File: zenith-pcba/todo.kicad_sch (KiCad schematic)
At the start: 2 parts, among them U1 XC7A50T-CSG325, U2 K4B4G1646E-BCNB

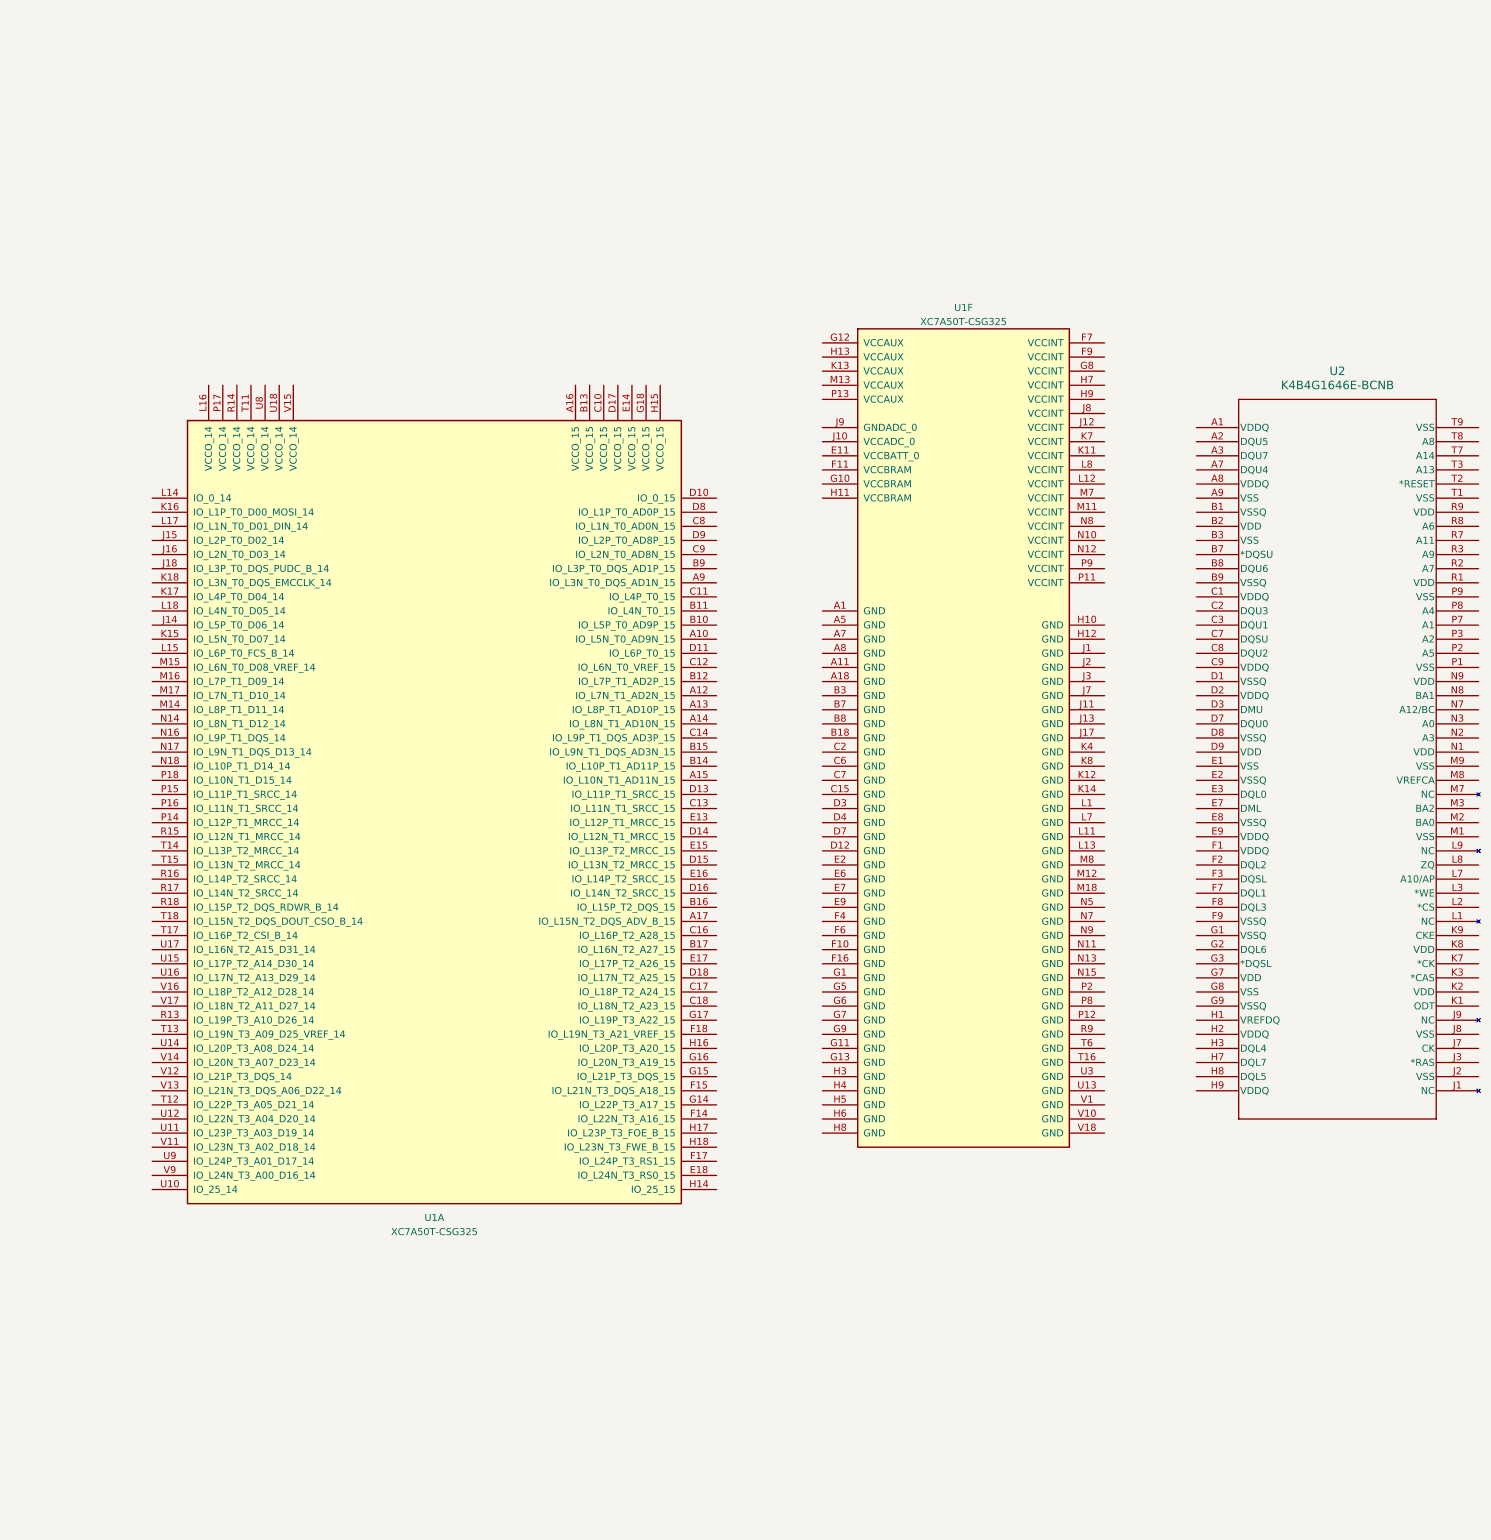
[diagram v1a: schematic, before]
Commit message: chore(pcba): import din connectors
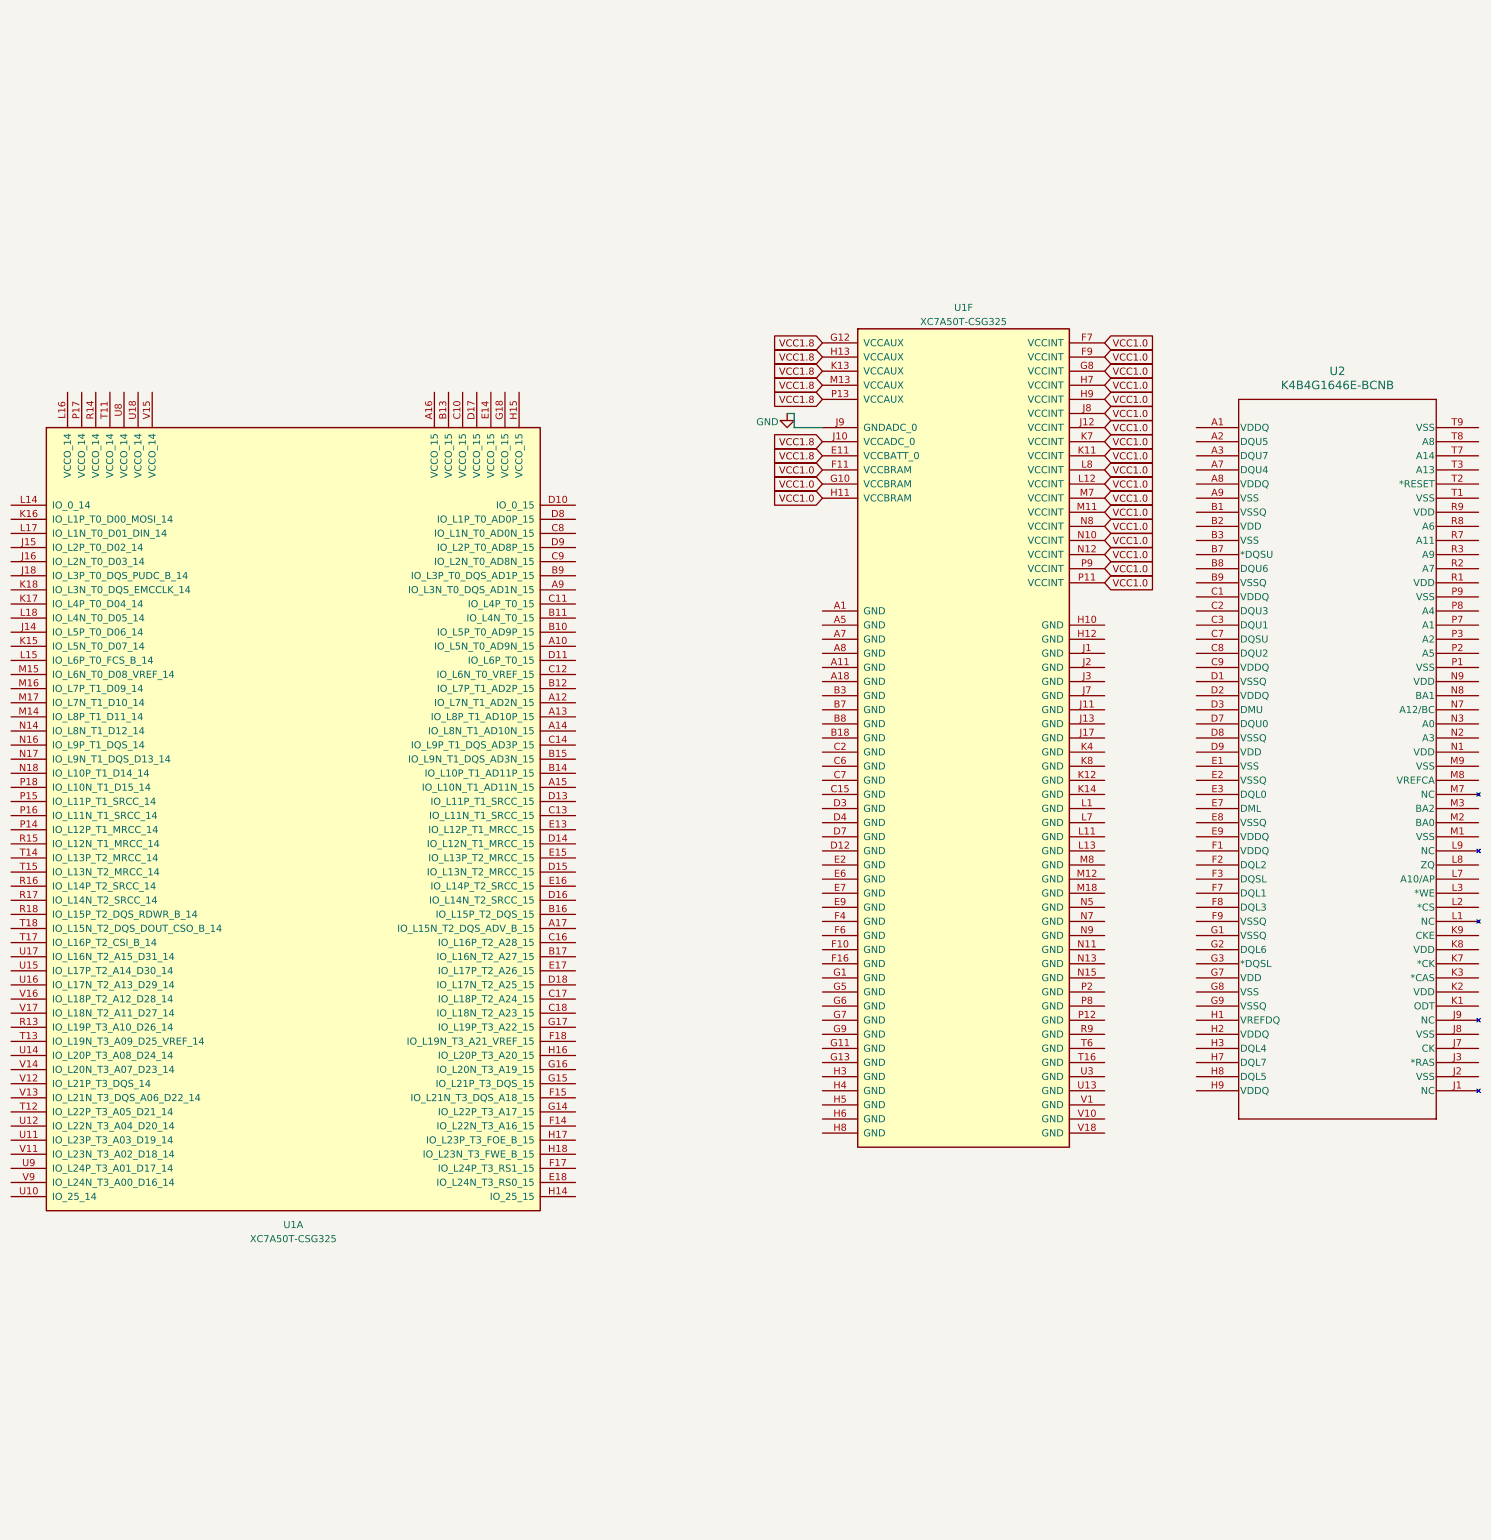
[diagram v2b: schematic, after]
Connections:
- net VCC1.8: now reaches U1.E11 (VCCBATT_0)
- net VCC1.8: now also U1.G12 (VCCAUX), U1.H13 (VCCAUX), U1.J10 (VCCADC_0), U1.K13 (VCCAUX), U1.M13 (VCCAUX), U1.P13 (VCCAUX)
- net VCC1.0: now reaches U1.F11 (VCCBRAM)
- net VCC1.0: now also U1.F7 (VCCINT), U1.F9 (VCCINT), U1.G10 (VCCBRAM), U1.G8 (VCCINT), U1.H11 (VCCBRAM), U1.H7 (VCCINT), U1.H9 (VCCINT), U1.J12 (VCCINT), U1.J8 (VCCINT), U1.K11 (VCCINT), U1.K7 (VCCINT), U1.L12 (VCCINT), U1.L8 (VCCINT), U1.M11 (VCCINT), U1.M7 (VCCINT), U1.N10 (VCCINT), U1.N12 (VCCINT), U1.N8 (VCCINT), U1.P11 (VCCINT), U1.P9 (VCCINT)
- net GND: now reaches U1.J9 (GNDADC_0)
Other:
- moved on the sheet: U1A

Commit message: feat(pcba): migrate to kintex fpga
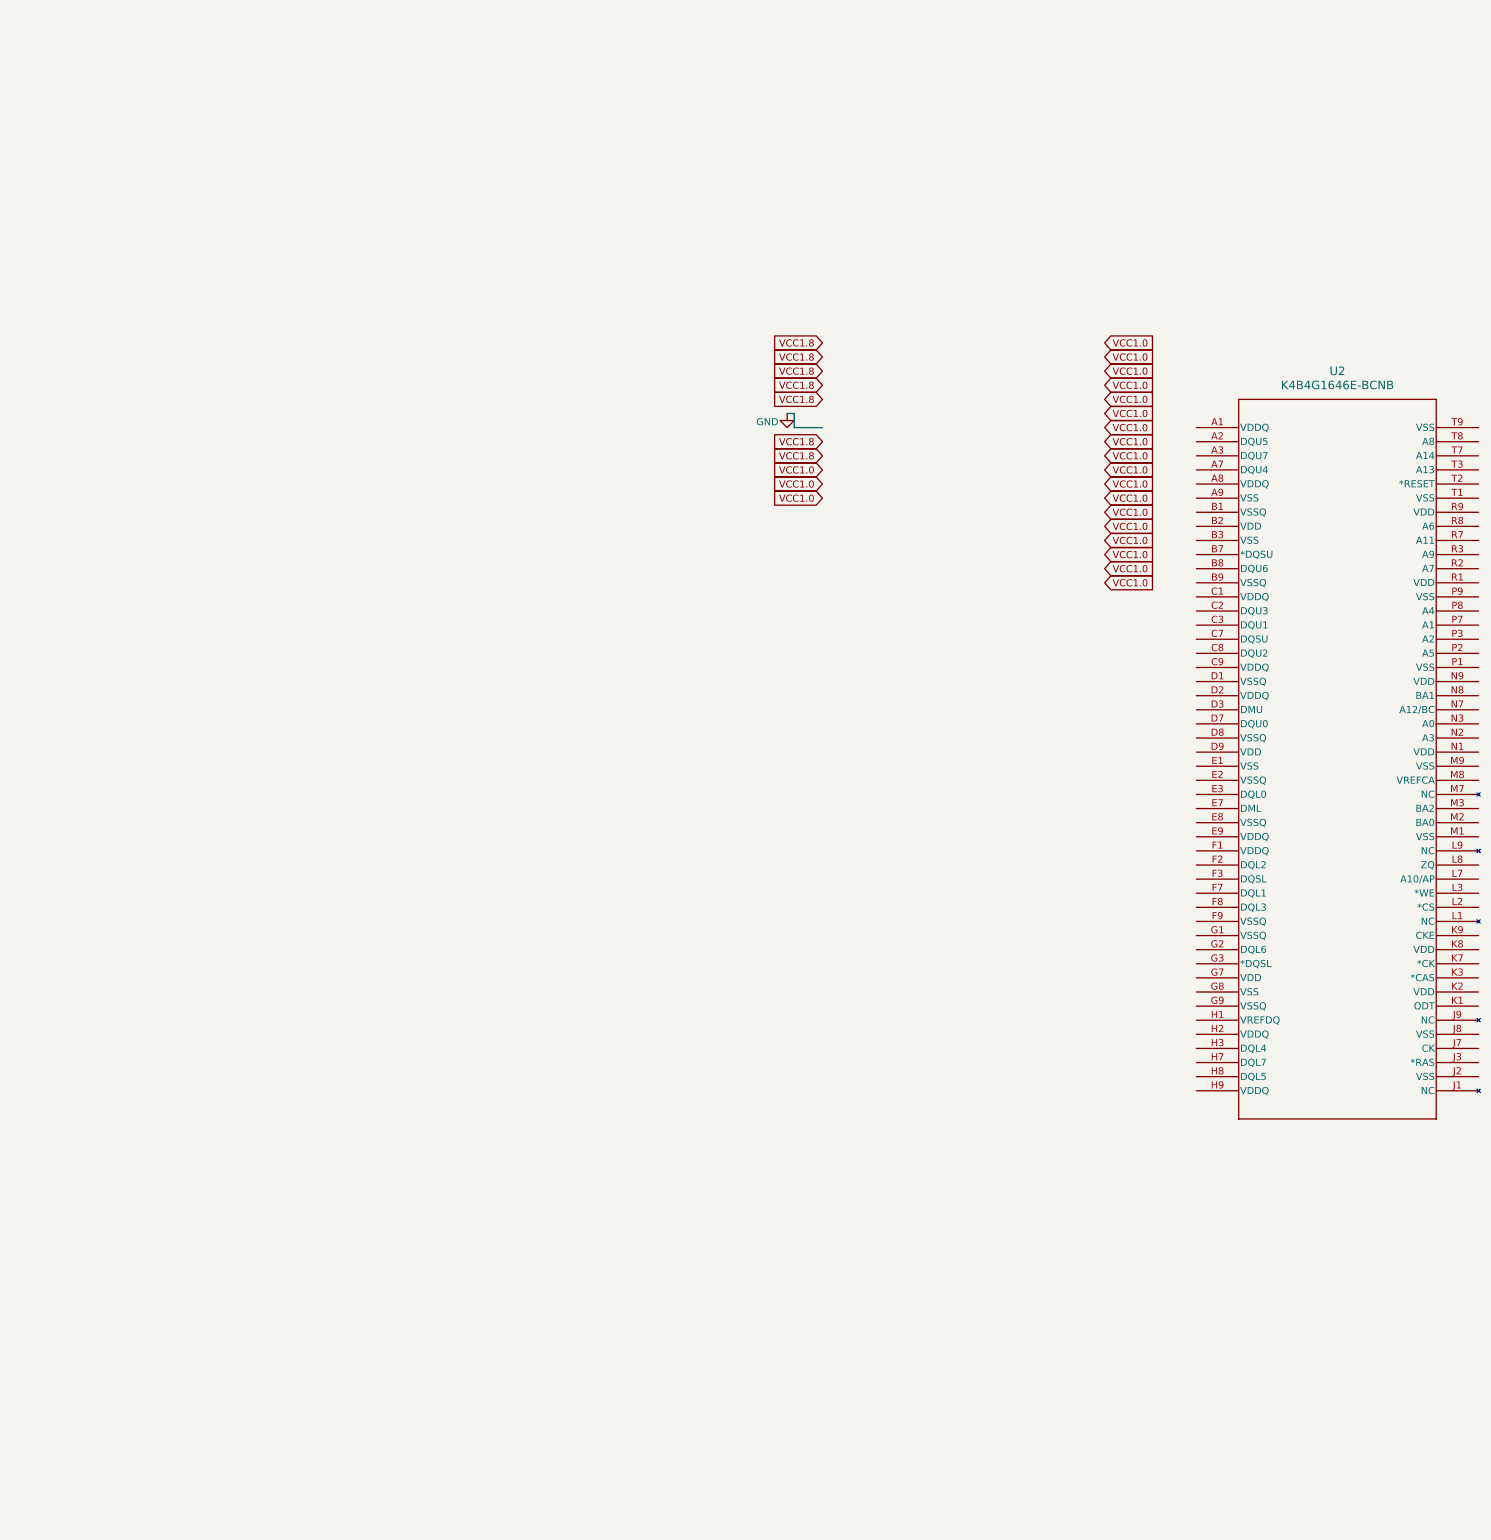
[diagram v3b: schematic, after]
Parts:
- removed U1: XC7A50T-CSG325, Package_BGA:Xilinx_CSG325, symbol FPGA_Xilinx_Artix7:XC7A50T-CSG325
